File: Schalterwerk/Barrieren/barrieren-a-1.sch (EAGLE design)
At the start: 76 parts, among them Q1 BSS84, Q2 BSS84, Q3 BSS84, Q4 BSS84, Q5 BSS84, Q6 BSS84, X1 PHNX_4P_350CONN_1984989_PXC, X2 PHNX_4P_350CONN_1984989_PXC, X3 PHNX_4P_350CONN_1984989_PXC, X4 PHNX_4P_350CONN_1984989_PXC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

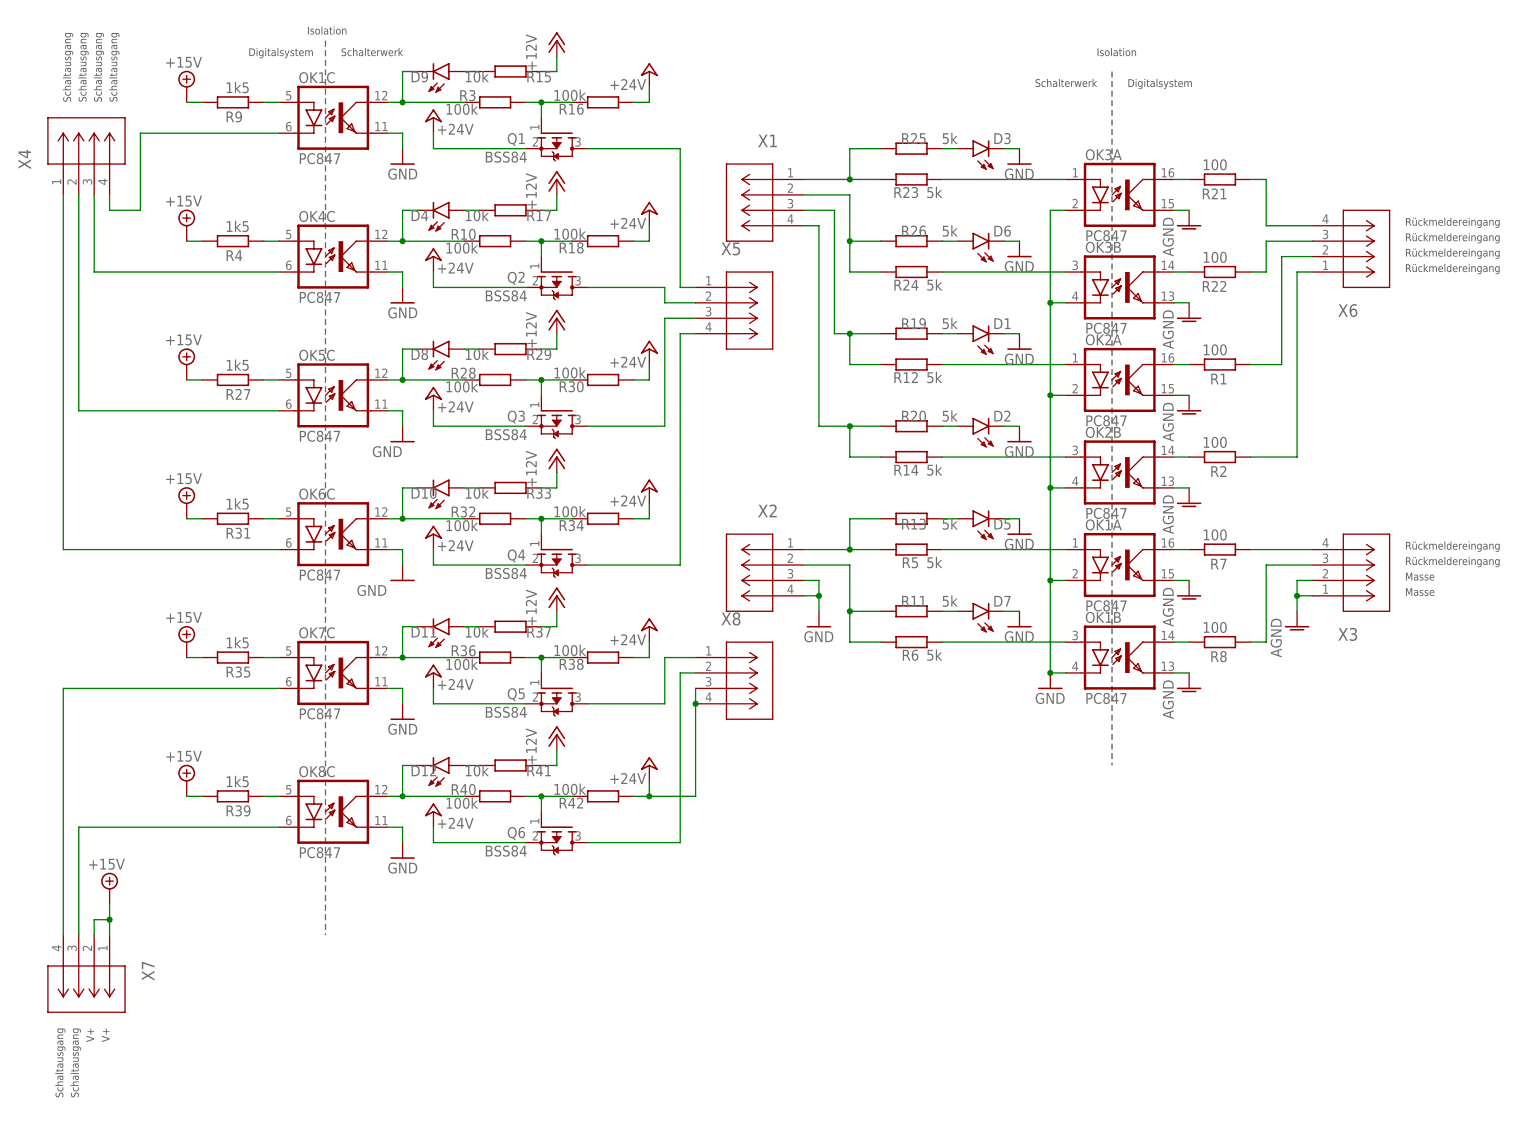
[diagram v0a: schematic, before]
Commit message: Places connectors and adds labeling.
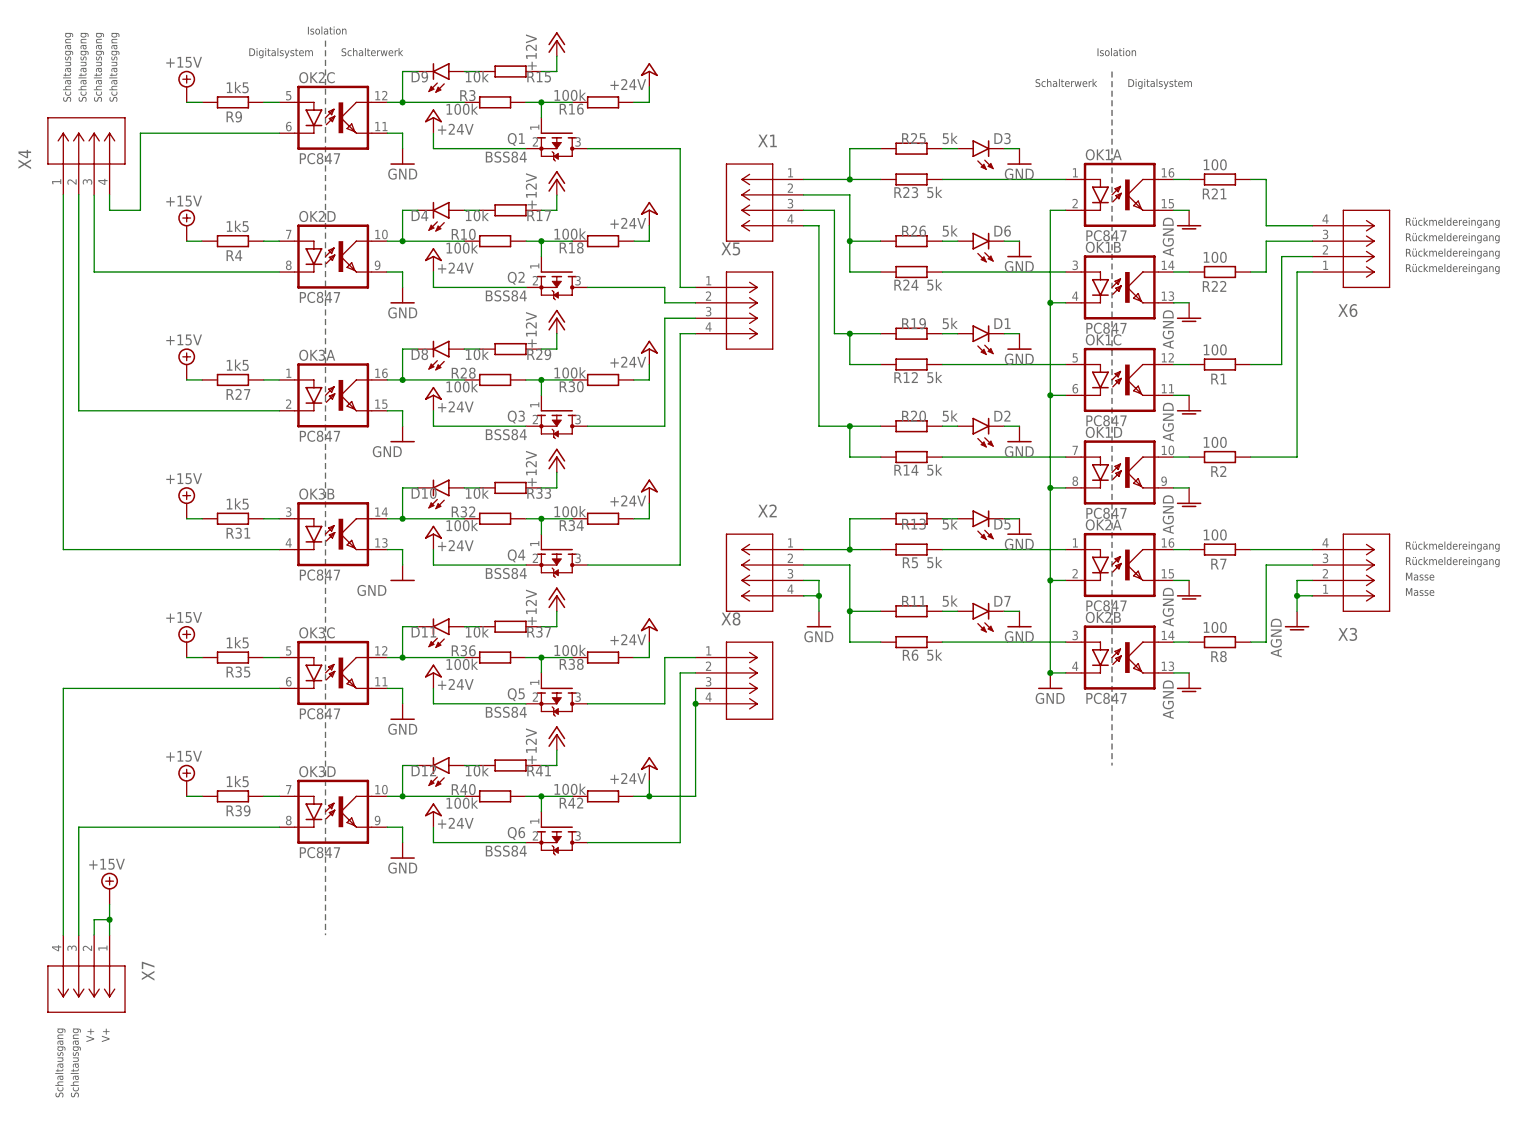
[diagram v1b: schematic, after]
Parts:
- removed OK4, OK5, OK6, OK7, OK8: PC847, optocoupler:PC847
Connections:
- net AGND: now also OK1C.EMIT, OK1D.EMIT; no longer OK3A.EMIT, OK3B.EMIT
- net GND: now also OK1C.C, OK1D.C, OK2C.EMIT, OK2D.EMIT, OK3A.EMIT, OK3B.EMIT, OK3C.EMIT, OK3D.EMIT; no longer OK1C.EMIT, OK3A.C, OK3B.C, OK4C.EMIT, OK5C.EMIT, OK6C.EMIT, OK7C.EMIT, OK8C.EMIT
- net N$10: now also OK1C.A; no longer OK2A.A
- net N$13: now also OK2D.COL; no longer OK4C.COL
- net N$15: now also OK3A.A; no longer OK5C.A
- net N$16: now also OK1D.A; no longer OK2B.A
- net N$19: now also OK2A.COL; no longer OK1A.COL
- net N$2: now also OK2A.A; no longer OK1A.A
- net N$20: now also OK3A.COL; no longer OK5C.COL
- net N$21: now also OK2B.COL; no longer OK1B.COL
- net N$23: now also OK3B.A; no longer OK6C.A
- net N$30: now also OK1A.COL; no longer OK3A.COL
- net N$31: now also OK2C.COL; no longer OK1C.COL
- net N$32: now also OK1B.COL; no longer OK3B.COL
- net N$33: now also OK1A.A; no longer OK3A.A
- net N$34: now also OK3B.COL; no longer OK6C.COL
- net N$35: now also OK1B.A; no longer OK3B.A
- net N$41: now also OK3C.A; no longer OK7C.A
- net N$43: now also OK3C.COL; no longer OK7C.COL
- net N$45: now also OK3D.A; no longer OK8C.A
- net N$47: now also OK3D.COL; no longer OK8C.COL
- net N$5: now also OK2C.A; no longer OK1C.A
- net N$6: now also OK1C.COL; no longer OK2A.COL
- net N$7: now also OK2B.A; no longer OK1B.A
- net N$8: now also OK2D.A; no longer OK4C.A
- net N$9: now also OK1D.COL; no longer OK2B.COL
- net NX3: now also OK2D.C; no longer OK4C.C
- net NX45: now also OK2C.C; no longer OK1C.C
- net NX6: now also OK3A.C; no longer OK5C.C
- net NX7: now also OK3B.C; no longer OK6C.C
- net NX8: now also OK3C.C; no longer OK7C.C
- net NX9: now also OK3D.C; no longer OK8C.C
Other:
- moved on the sheet: OK1A, OK1B, OK1C, OK2A, OK2B, OK3A, OK3B
